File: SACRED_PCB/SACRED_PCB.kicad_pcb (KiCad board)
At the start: 2 copper layers, 38 parts, among them J1 Screw_Terminal_01x02, J10 Conn_01x14, J11 Conn_01x13, J12 Screw_Terminal_01x04, J13 Screw_Terminal_01x02, J14 Conn_01x16, J2 Analog 0, J4 Stepper 0, J5 Stepper 1, J7 Stepper 2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

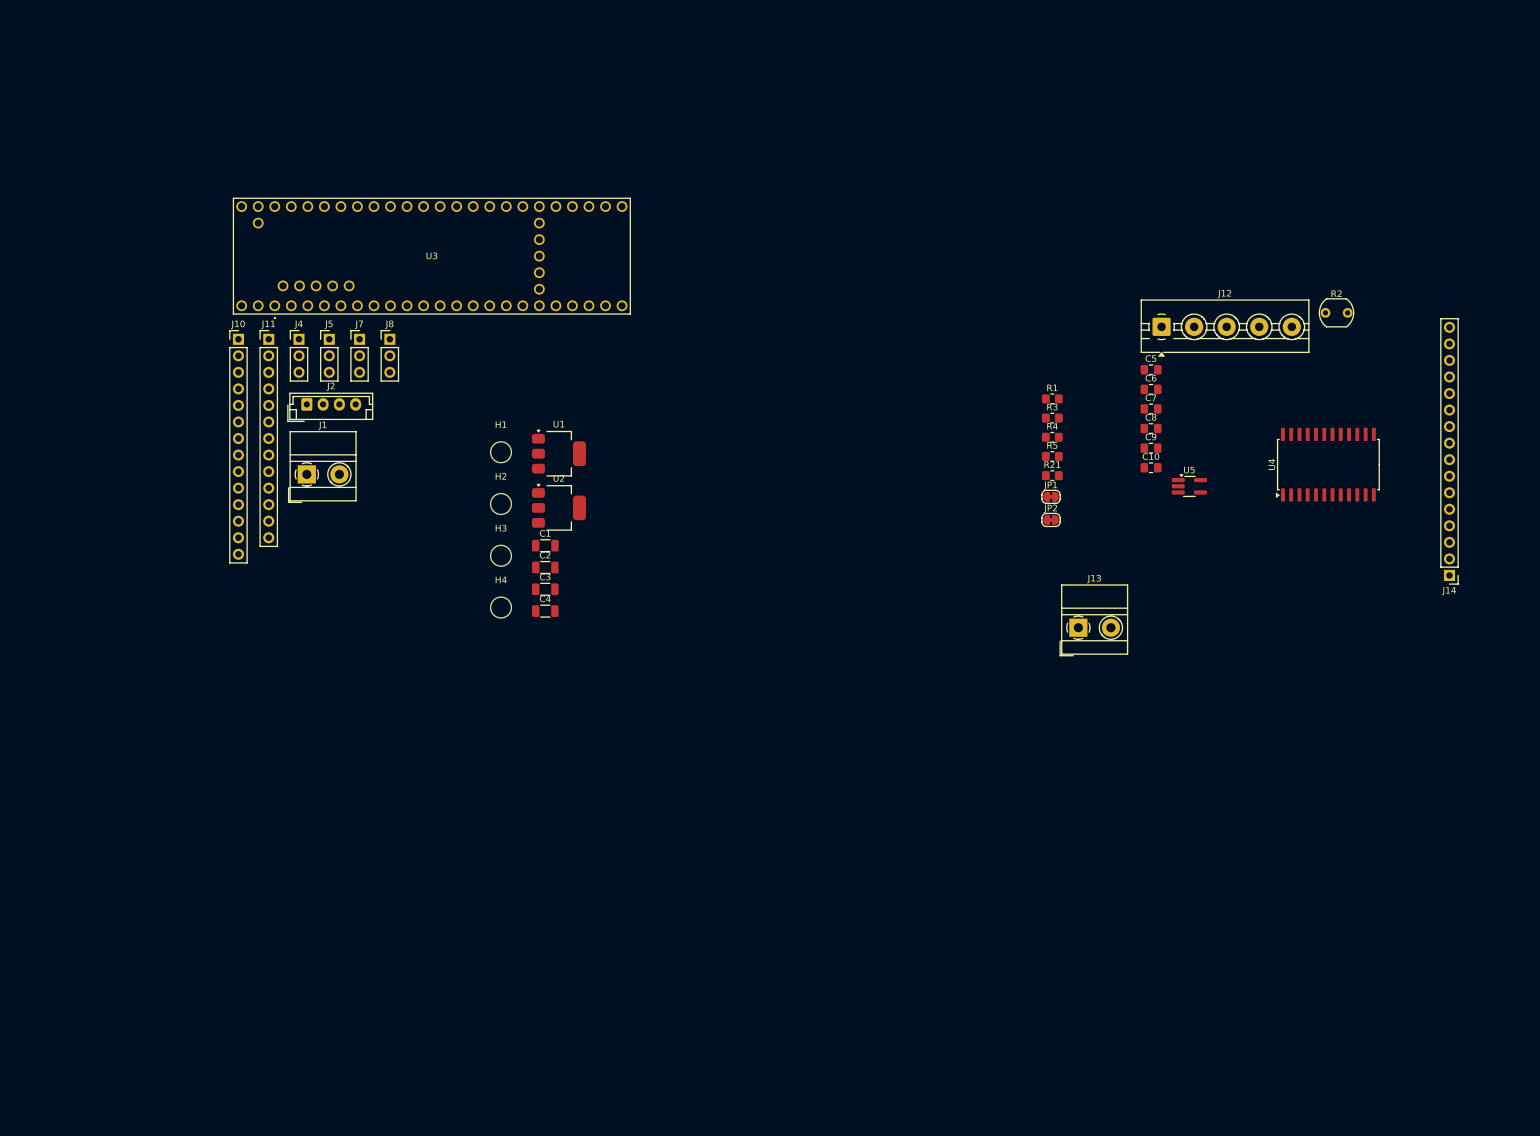
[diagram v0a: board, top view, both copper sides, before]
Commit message: Proper arm generation and PCB progress
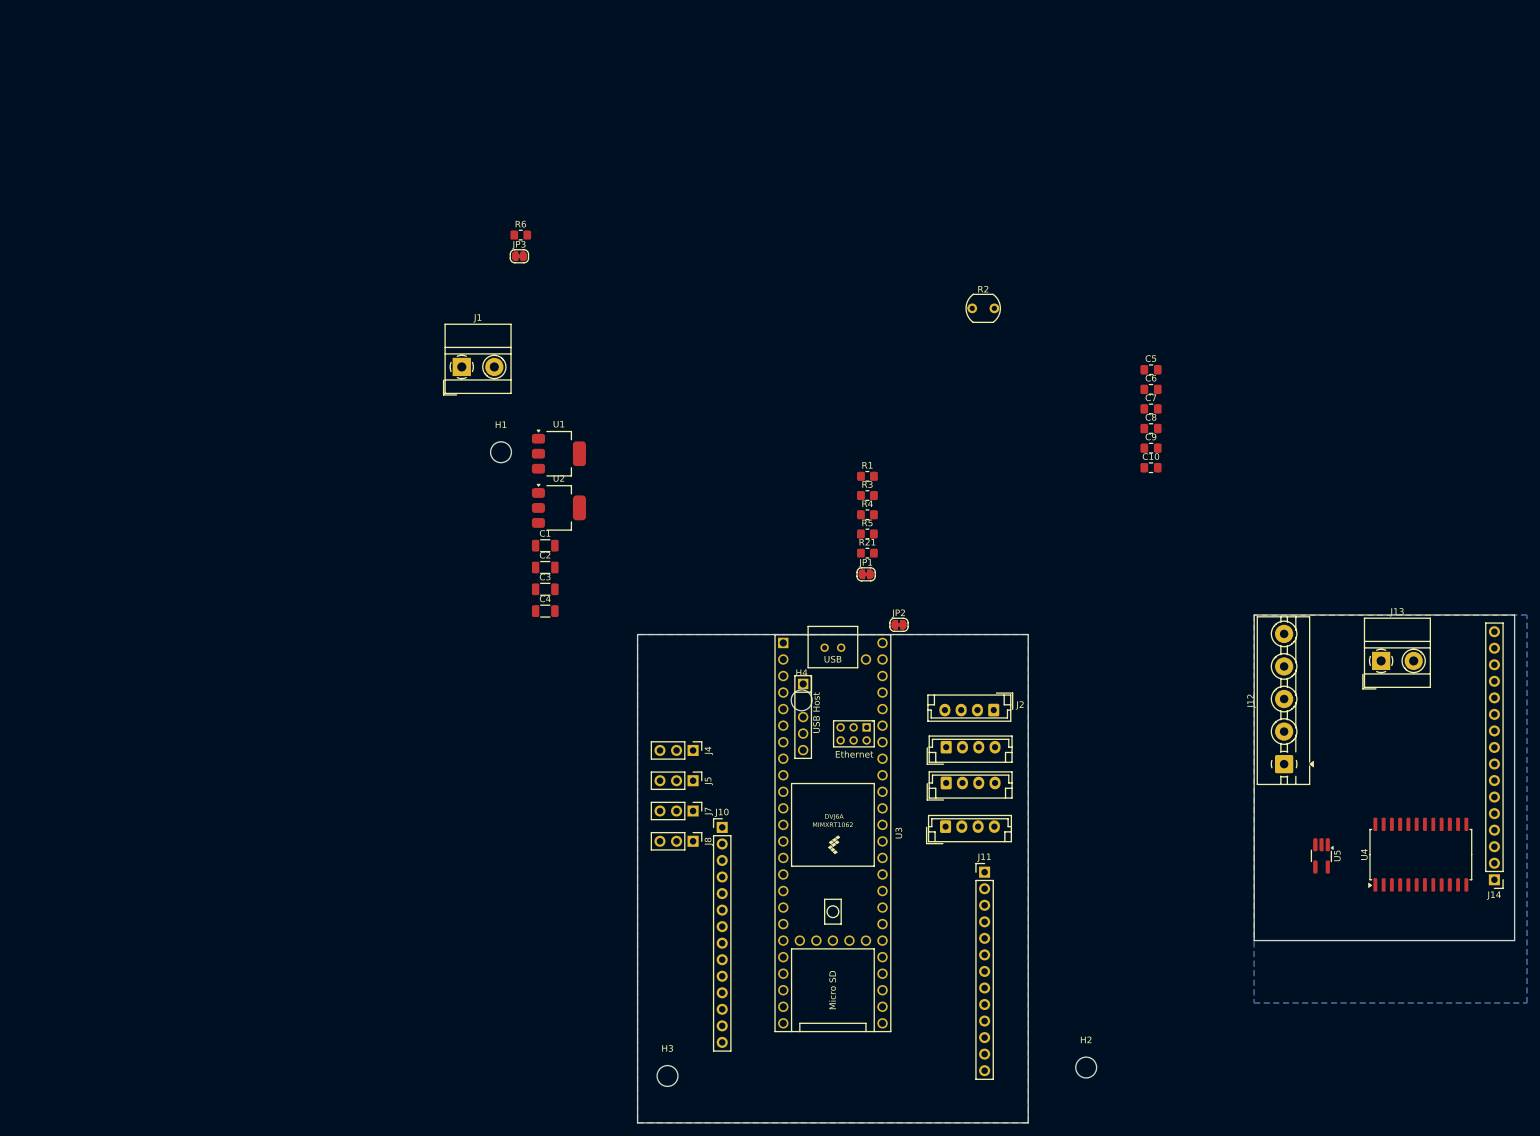
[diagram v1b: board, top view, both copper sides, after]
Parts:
- added J3: Analog 1, Connector_JST:JST_EH_B4B-EH-A_1x04_P2.50mm_Vertical, F.Cu at (145.2, 111.0)
- added J6: Analog 2, Connector_JST:JST_EH_B4B-EH-A_1x04_P2.50mm_Vertical, F.Cu at (145.2, 116.5)
- added J9: Analog 3, Connector_JST:JST_EH_B4B-EH-A_1x04_P2.50mm_Vertical, F.Cu at (145.1, 123.2)
- added JP3: Solder _Bridge, Jumper:SolderJumper-2_P1.3mm_Bridged_RoundedPad1.0x1.5mm, F.Cu at (79.7, 35.6)
- added R6: 100k, Resistor_SMD:R_0805_2012Metric_Pad1.20x1.40mm_HandSolder, F.Cu at (79.8, 32.4)
- U3: footprint Teensy:TEENSY41 -> Teensy:Teensy41_2
- moved J11 137.1 mm to (151.1, 130.2)
- moved H2 124.8 mm to (166.7, 160.2)
- moved U3 117.9 mm to (127.8, 124.2), turned to -90 degrees
- moved J2 115.5 mm to (152.5, 105.3), turned to 180 degrees
- moved J10 105.6 mm to (110.8, 123.3)
- moved J8 90.1 mm to (106.3, 125.5), turned to -90 degrees
- moved J7 88.7 mm to (106.3, 120.8), turned to -90 degrees
- moved J5 87.9 mm to (106.3, 116.2), turned to -90 degrees
- moved J4 87.5 mm to (106.3, 111.5), turned to -90 degrees
- moved H3 83.9 mm to (102.4, 161.5)
- moved J12 69.7 mm to (197.1, 113.6), turned to 90 degrees
- moved U4 61.6 mm to (218.1, 127.5)
- moved U5 60.3 mm to (202.8, 127.7), turned to -90 degrees
- moved R2 54.3 mm to (149.2, 43.6)
- moved H4 48.3 mm to (123.0, 103.8)
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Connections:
- net /PinA_1 renamed /Pin_15
- net /PinA_10 renamed /Pin_36
- net /PinA_11 renamed /Pin_35
- net /PinA_12 renamed /Pin_34
- net /PinA_13 renamed /Pin_33
- net /PinA_4 renamed /Pin_GND
- net /PinA_5 renamed /Pin_41
- net /PinA_6 renamed /Pin_40
- net /PinA_7 renamed /Pin_39
- net /PinA_8 renamed /Pin_38
- net /PinA_9 renamed /Pin_37
- net /Pin_10 renamed /Pin_28
- net /Pin_11 renamed /Pin_29
- net /Pin_12 renamed /Pin_30
- net /Pin_5 renamed /Pin_3v3
- net /Pin_6 renamed /Pin_24
- net /Pin_7 renamed /Pin_25
- net /Pin_8 renamed /Pin_26
- net /Pin_9 renamed /Pin_27
- J10 pad 1: /Pin_1 -> /Pin_0
- J10 pad 13: /Pin_13 -> /Pin_31
- J10 pad 14: /Pin_14 -> /Pin_32
- J10 pad 2: /Pin_2 -> /Pin_1
- J10 pad 3: /Pin_3 -> /Pin_2
- J10 pad 4: /Pin_4 -> /Pin_3
- J11 pad 2: /PinA_2 -> /Pin_14
- J11 pad 3: /PinA_3 -> /Pin_13
- R2 pad 1: /Analog_0 -> Net-(JP3-B)
- U3 pad 2: /Pin_1 -> /Pin_0
- U3 pad 23: /Pin_13 -> /Pin_31
- U3 pad 24: /Pin_14 -> /Pin_32
- U3 pad 3: /Pin_2 -> /Pin_1
- U3 pad 35: /PinA_3 -> /Pin_13
- U3 pad 36: /PinA_2 -> /Pin_14
- U3 pad 4: /Pin_3 -> /Pin_2
- U3 pad 5: /Pin_4 -> /Pin_3
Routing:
- added copper zone on B.Cu, net GND
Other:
- board outline added: 134.7 x 78 mm

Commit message: PCB Rev 0.1
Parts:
- removed C10: 100nF, Capacitor_SMD:C_0805_2012Metric_Pad1.18x1.45mm_HandSolder
- removed R21: 3M, Resistor_SMD:R_0805_2012Metric_Pad1.20x1.40mm_HandSolder
- added H4: MountingHole, MountingHole:MountingHole_3.2mm_M3, F.Cu at (206.4, 119.1)
- added J15: Screw_Terminal_01x04, TerminalBlock_Phoenix:TerminalBlock_Phoenix_MKDS-1,5-3-5.08_1x03_P5.08mm_Horizontal, F.Cu at (143.2, 129.8)
- added J16: Conn_01x04, Connector_PinHeader_2.54mm:PinHeader_1x04_P2.54mm_Vertical, F.Cu at (107.9, 96.7)
- added J17: Analog 0, Connector_PinHeader_2.54mm:PinHeader_1x05_P2.54mm_Vertical, F.Cu at (225.1, 126.3)
- added J18: Conn_01x16, Connector_PinHeader_2.54mm:PinHeader_1x08_P2.54mm_Vertical, F.Cu at (206.8, 112.0)
- J1: footprint TerminalBlock_MetzConnect:TerminalBlock_MetzConnect_Type011_RT05502HBWC_1x02_P5.00mm_Horizontal -> TerminalBlock_Phoenix:TerminalBlock_Phoenix_MKDS-1,5-2_1x02_P5.00mm_Horizontal
- J10: value Conn_01x14 -> Conn_01x11; footprint Connector_PinHeader_2.54mm:PinHeader_1x14_P2.54mm_Vertical -> Connector_PinHeader_2.54mm:PinHeader_1x11_P2.54mm_Vertical
- J12: footprint TerminalBlock:TerminalBlock_MaiXu_MX126-5.0-05P_1x05_P5.00mm -> TerminalBlock_Phoenix:TerminalBlock_Phoenix_MKDS-1,5-3-5.08_1x03_P5.08mm_Horizontal
- J14: footprint Connector_PinHeader_2.54mm:PinHeader_1x16_P2.54mm_Vertical -> Connector_PinHeader_2.54mm:PinHeader_1x08_P2.54mm_Vertical
- J2, J3, J6, J9: footprint Connector_JST:JST_EH_B4B-EH-A_1x04_P2.50mm_Vertical -> Connector_PinHeader_2.54mm:PinHeader_1x05_P2.54mm_Vertical
- R2: footprint OptoDevice:R_LDR_5.1x4.3mm_P3.4mm_Vertical -> Potentiometer_THT:Potentiometer_Bourns_3296W_Vertical
- moved R6 167.6 mm to (211.6, 136.0), turned to 180 degrees
- moved JP3 167.2 mm to (211.6, 138.3), turned to 180 degrees
- moved C4 127.1 mm to (205.7, 125.4), turned to 90 degrees
- moved U2 124.8 mm to (198.5, 127.8), turned to -90 degrees
- moved J1 124.0 mm to (143.8, 152.8), turned to 90 degrees
- moved C3 119.3 mm to (197.6, 121.9)
- moved R2 107.2 mm to (202.4, 136.7)
- moved H4 106.3 mm to (224.1, 136.7)
- moved R3 105.0 mm to (220.8, 130.0), turned to 90 degrees
- moved R5 95.1 mm to (217.7, 121.6), turned to -90 degrees
- moved R4 94.5 mm to (217.7, 117.5), turned to -90 degrees
- moved R1 94.2 mm to (215.4, 115.2), turned to -90 degrees
- moved JP1 93.3 mm to (220.2, 117.5), turned to 90 degrees
- moved U1 92.0 mm to (141.5, 139.1), turned to 90 degrees
- moved H2 89.4 mm to (102.1, 98.4)
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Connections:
- J1 pad 1: +12V -> GND
- J1 pad 2: GND -> +12V
- J10 pad 1: /Pin_0 -> /Pin_12
- J10 pad 10: /Pin_28 -> /Pin_31
- J10 pad 11: /Pin_29 -> /Pin_32
- J10 pad 2: /Pin_1 -> /Pin_3v3
- J10 pad 3: /Pin_2 -> /Pin_24
- J10 pad 4: /Pin_3 -> /Pin_25
- J10 pad 5: /Pin_3v3 -> /Pin_26
- J10 pad 6: /Pin_24 -> /Pin_27
- J10 pad 7: /Pin_25 -> /Pin_28
- J10 pad 8: /Pin_26 -> /Pin_29
- J10 pad 9: /Pin_27 -> /Pin_30
- J12 pad 1: +12V -> GND
- J12 pad 2: +5V -> +12V
- J12 pad 3: +3.3V -> +5V
- J4 pad 1: /Stepper_EN -> +5V
- J5 pad 1: /Stepper_EN -> +5V
- J7 pad 1: /Stepper_EN -> +5V
- J8 pad 1: /Stepper_EN -> +5V
- U3 pad 11: /Stepper_2_STEP -> /Stepper_1_DIR
- U3 pad 12: /Stepper_2_DIR -> /Stepper_0_STEP
- U3 pad 13: /Stepper_3_STEP -> /Stepper_0_DIR
- U3 pad 14: /Stepper_3_DIR -> /Pin_12
- U3 pad 6: /Stepper_EN -> /Stepper_3_DIR
- U3 pad 7: /Stepper_0_DIR -> /Stepper_3_STEP
- U3 pad 8: /Stepper_0_STEP -> /Stepper_2_DIR
- U3 pad 9: /Stepper_1_DIR -> /Stepper_2_STEP
- U4 pad 16: Net-(J14-Pin_16) -> Net-(J18-Pin_8)
- U4 pad 17: Net-(J14-Pin_15) -> Net-(J18-Pin_7)
- U4 pad 18: Net-(J14-Pin_14) -> Net-(J18-Pin_6)
- U4 pad 19: Net-(J14-Pin_13) -> Net-(J18-Pin_5)
- U4 pad 20: Net-(J14-Pin_12) -> Net-(J18-Pin_4)
- U4 pad 21: Net-(J14-Pin_11) -> Net-(J18-Pin_3)
- U4 pad 22: Net-(J14-Pin_10) -> Net-(J18-Pin_2)
- U4 pad 23: Net-(J14-Pin_9) -> Net-(J18-Pin_1)
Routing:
- net +5V: track 0.00 -> 108.6 mm, vias 0 -> 2
- net +12V: track 0.00 -> 70.0 mm, vias 0 -> 1
- net /MUX_3: track 0.00 -> 67.3 mm, vias 0 -> 1
- net /MUX_2: track 0.00 -> 63.0 mm, vias 0 -> 1
- net /MUX_1: track 0.00 -> 58.8 mm, vias 0 -> 1
- net /MUX_0: track 0.00 -> 54.8 mm, vias 0 -> 1
- net GND: track 0.00 -> 54.7 mm, vias 0 -> 8
- net /Analog_0: track 0.00 -> 35.0 mm, vias 0 -> 1
- net Net-(U4-COM): track 0.00 -> 25.0 mm
- net +3.3V: track 0.00 -> 23.6 mm, vias 0 -> 2
- net Net-(U5--): track 0.00 -> 14.4 mm, vias 0 -> 1
- net Net-(JP3-B): track 0.00 -> 10.9 mm, vias 0 -> 1
- net /Stepper_0_DIR: track 0.00 -> 9.00 mm
- net /Stepper_3_STEP: track 0.00 -> 8.78 mm
- net /Stepper_1_STEP: track 0.00 -> 8.77 mm
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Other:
- board size 134.7 x 78 mm -> 130.2 x 66 mm

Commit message: PCB with rivets
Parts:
- added H5: MountingHole, MountingHole:MountingHole_3.2mm_M3, F.Cu at (3.48, 3.48)
- R1, R3, R4, R5, R6: footprint Resistor_SMD:R_0805_2012Metric_Pad1.20x1.40mm_HandSolder -> Resistor_SMD:R_0603_1608Metric_Pad0.98x0.95mm_HandSolder
- moved JP2 1.53 mm to (218.9, 122.2)
- moved R5 1.53 mm to (216.3, 122.2)
- moved JP1 1.53 mm to (218.8, 118.0)
- moved R4 1.53 mm to (216.3, 118.0)
- moved C3 1.30 mm to (198.9, 121.9)
- moved R1 1.20 mm to (214.5, 114.4)
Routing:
- net +5V: track 108.6 -> 117.6 mm, vias 2 -> 3
- net +3.3V: track 23.6 -> 31.2 mm
- net GND: track 54.7 -> 60.5 mm
- net /Analog_0: track 35.0 -> 38.2 mm
- net Net-(U5--): track 14.4 -> 16.1 mm
- net /MUX_0: track 54.8 -> 53.7 mm
- net +12V: track 70.0 -> 70.9 mm
- net /MUX_1: track 58.8 -> 58.0 mm
- net Net-(J14-Pin_5): track 4.69 -> 3.86 mm
- net Net-(J18-Pin_7): track 6.60 -> 5.81 mm
- net Net-(U4-COM): track 25.0 -> 24.2 mm
- net /MUX_3: track 67.3 -> 67.9 mm
- net Net-(J18-Pin_8): track 7.92 -> 7.31 mm
- net Net-(J14-Pin_2): track 7.14 -> 6.54 mm
- net /MUX_2: track 63.0 -> 63.5 mm
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
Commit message: Saving more
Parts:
- removed C3, C4: 10uF, Capacitor_SMD:C_1206_3216Metric
- removed C5, C7: 100nF, Capacitor_SMD:C_0805_2012Metric_Pad1.18x1.45mm_HandSolder
- removed C6, C8: 10uF, Capacitor_SMD:C_0805_2012Metric_Pad1.18x1.45mm_HandSolder
- removed C9: 1pF, Capacitor_SMD:C_0805_2012Metric_Pad1.18x1.45mm_HandSolder
- removed H4 (x2), H5: MountingHole, MountingHole:MountingHole_3.2mm_M3
- removed J12: Screw_Terminal_01x04, TerminalBlock_Phoenix:TerminalBlock_Phoenix_MKDS-1,5-3-5.08_1x03_P5.08mm_Horizontal
- removed J13: Screw_Terminal_01x02, TerminalBlock_MetzConnect:TerminalBlock_MetzConnect_Type011_RT05502HBWC_1x02_P5.00mm_Horizontal
- removed J14, J18: Conn_01x16, Connector_PinHeader_2.54mm:PinHeader_1x08_P2.54mm_Vertical
- removed J17: Analog 0, Connector_PinHeader_2.54mm:PinHeader_1x05_P2.54mm_Vertical
- removed JP1, JP2, JP3: Solder _Bridge, Jumper:SolderJumper-2_P1.3mm_Bridged_RoundedPad1.0x1.5mm
- removed R1, R4, R5, R6: 100k, Resistor_SMD:R_0603_1608Metric_Pad0.98x0.95mm_HandSolder
- removed R2: R_Trim, Potentiometer_THT:Potentiometer_Bourns_3296W_Vertical
- removed R3: 10k, Resistor_SMD:R_0603_1608Metric_Pad0.98x0.95mm_HandSolder
- removed U2: AMS1117-3.3, Package_TO_SOT_SMD:SOT-223-3_TabPin2
- removed U4: CD74HCT4067QM96Q, Package_SO:SOIC-24W_7.5x15.4mm_P1.27mm
- removed U5: OPA607Q1, Package_TO_SOT_SMD:TSOT-23-5_HandSoldering
- moved J1 41.5 mm to (139.0, 111.6)
- moved C2 41.5 mm to (130.8, 98.6)
- moved J16 41.5 mm to (103.1, 55.5)
- moved C1 41.5 mm to (142.5, 99.8)
- moved J10 41.5 mm to (103.1, 86.7)
- moved J3 41.5 mm to (128.0, 65.0)
- moved J9 41.5 mm to (128.0, 72.3)
- moved U1 41.5 mm to (136.7, 97.9)
- moved H2 41.5 mm to (97.3, 57.2)
- moved J11 41.5 mm to (126.8, 81.7)
- moved J15 41.5 mm to (138.4, 88.6)
- moved J2 41.5 mm to (128.0, 61.4)
- moved J4 41.5 mm to (96.9, 81.7)
- moved J5 41.5 mm to (96.9, 77.0)
- moved J8 41.5 mm to (96.9, 67.8)
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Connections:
- J11 pad 4: /Pin_GND -> GND
- U3 pad 34: /Pin_GND -> GND
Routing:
- net GND: track 60.5 -> 16.2 mm, vias 8 -> 2
- net /MUX_3: track 67.9 -> 29.9 mm, vias 1 -> 0
- net /MUX_2: track 63.5 -> 26.9 mm, vias 1 -> 0
- net /MUX_1: track 58.0 -> 24.3 mm, vias 1 -> 0
- net /Analog_0: track 38.2 -> 5.37 mm, vias 1 -> 0
- net +5V: track 117.6 -> 85.6 mm, vias 3 -> 2
- net /MUX_0: track 53.7 -> 21.9 mm, vias 1 -> 0
- net +3.3V: track 31.2 -> 0.00 mm, vias 2 -> 0
- net Net-(U4-COM): track 24.2 -> 0.00 mm
- net +12V: track 70.9 -> 47.5 mm
- net Net-(U5--): track 16.1 -> 0.00 mm, vias 1 -> 0
- net Net-(JP3-B): track 10.4 -> 0.00 mm, vias 1 -> 0
- net Net-(J14-Pin_1): track 8.09 -> 0.00 mm, vias 1 -> 0
- net Net-(JP1-A): track 7.49 -> 0.00 mm
- net Net-(J18-Pin_8): track 7.31 -> 0.00 mm, vias 1 -> 0
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- added copper zone on F.Cu, net GND
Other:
- board size 130.2 x 66 mm -> 52.9 x 63 mm
